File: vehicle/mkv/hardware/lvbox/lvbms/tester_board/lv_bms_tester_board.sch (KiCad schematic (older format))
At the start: 13 parts, among them Q1 SQM110P06, Q2 MMBF170, Q3 SQM110P06, U3 redcube-7461057, U4 redcube-7461057

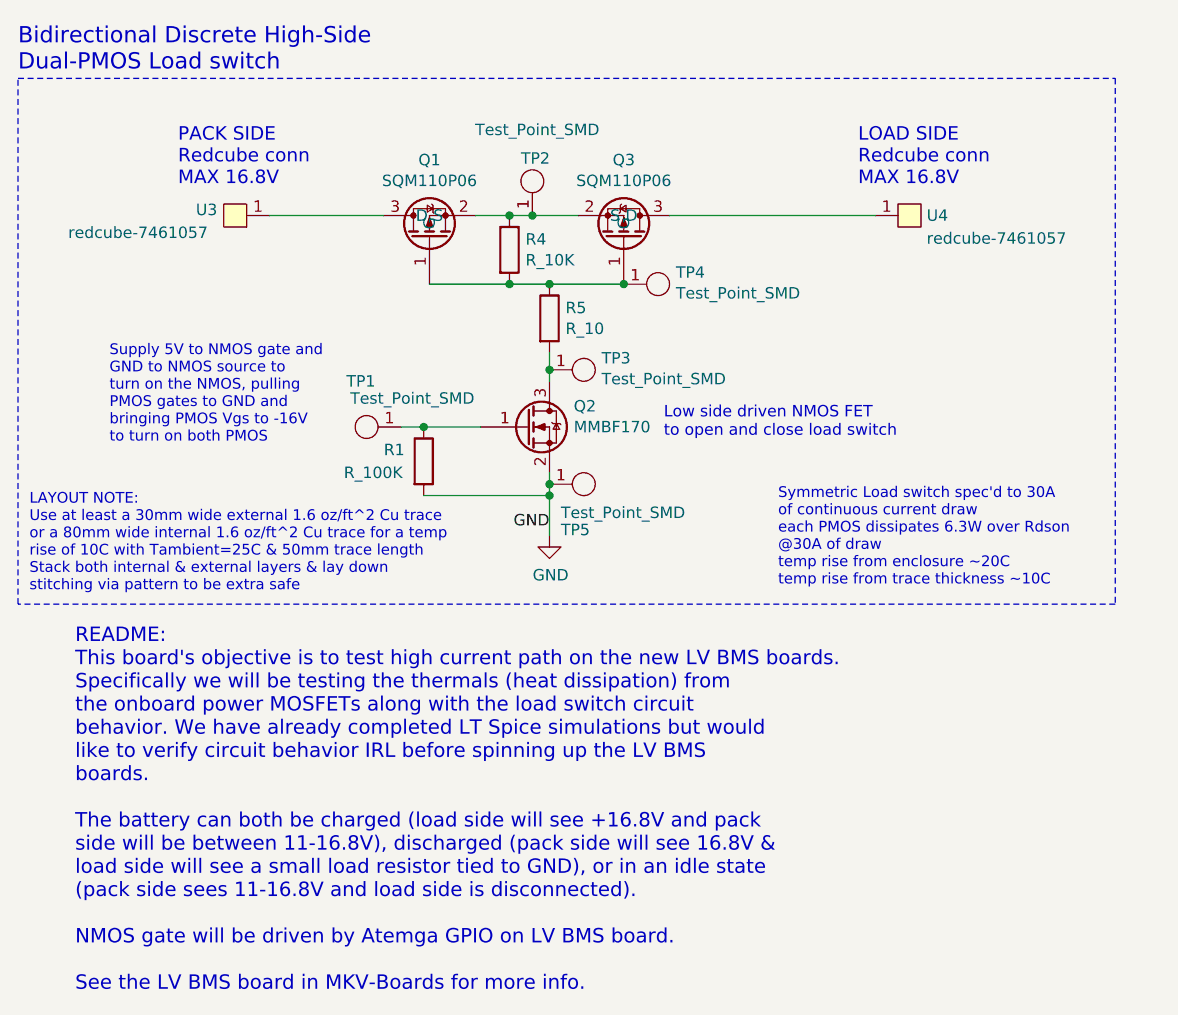
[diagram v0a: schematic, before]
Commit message: Updates based on feedback to LV BMS tester board
Also fixes smudge/clean
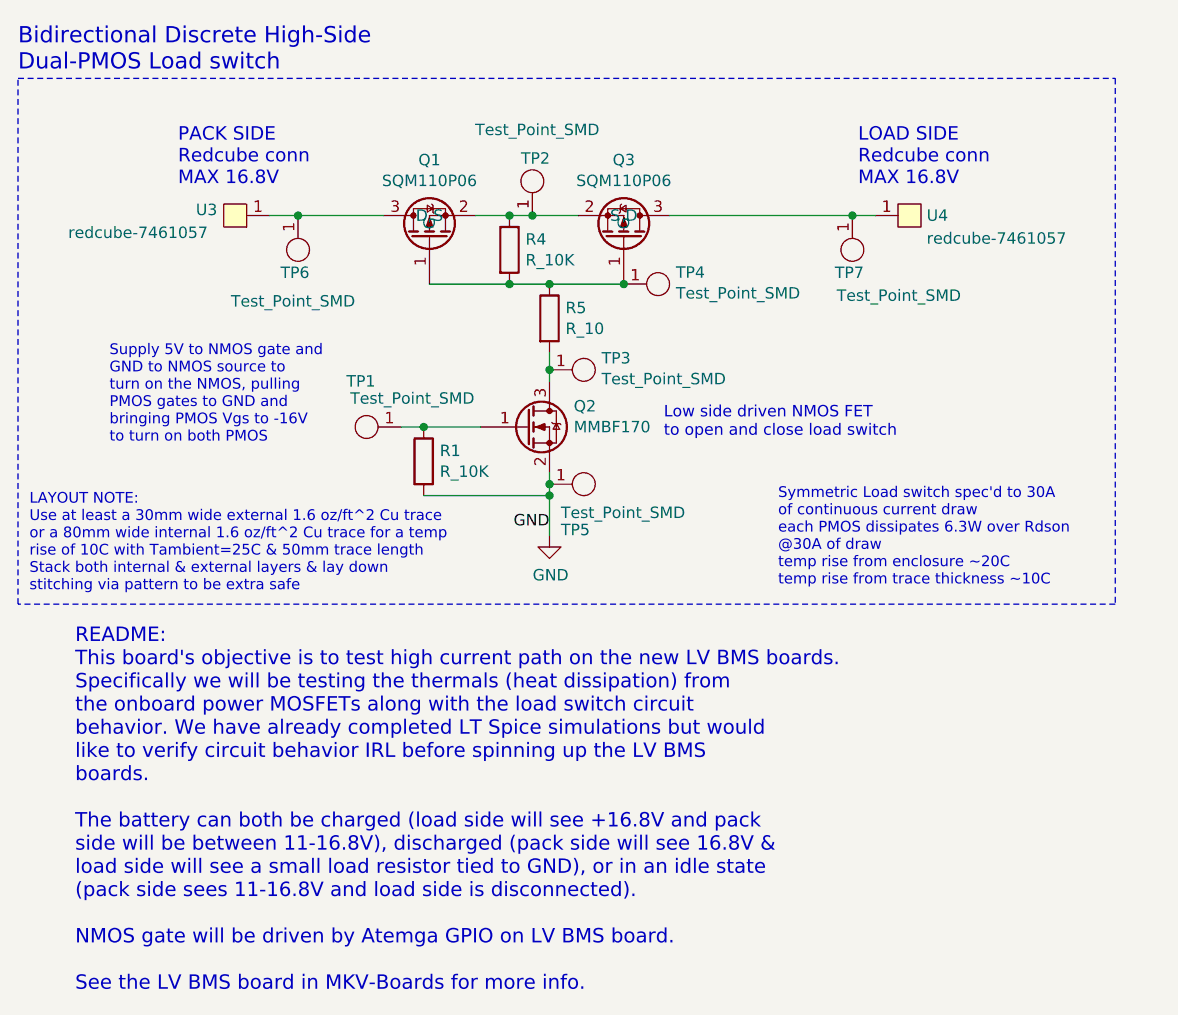
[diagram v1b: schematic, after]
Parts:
- removed R1: R_100K, formula:R_0805_OEM, symbol formula:R_100K
- added R1: R_10K, formula:R_0805_OEM, symbol formula:R_10K
- added TP6, TP7: Test_Point_SMD, TestPoint:TestPoint_Pad_D1.5mm, symbol formula:Test_Point_SMD
- TP1, TP5: footprint TestPoint:TestPoint_Pad_D1.5mm -> TestPoint:TestPoint_Pad_2.0x2.0mm
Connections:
- net GND: now also R1.2
- net at Q1.3 (D), U3.1: now also TP6.1
- net at Q3.3 (D), U4.1: now also TP7.1
- net at Q2.1 (G), TP1.1: now also R1.1
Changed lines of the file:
@@
 $EndComp
 Wire Wire Line
-	3425 1400 4325 1400
-Wire Wire Line
-	1675 1400 2175 1400
+	3425 1400 4225 1400
+Wire Wire Line
+	1675 1400 1800 1400
 $Comp
 L formula:R_10K R4
@@
 	1    0    0    -1
 $EndComp
-Wire Wire Line
-	2600 2325 2350 2325
 $Comp
 L formula:Test_Point_SMD TP1
@@
 F 0 "TP1" V 2400 2450 50  0000 C CNN
 F 1 "Test_Point_SMD" V 2325 2225 50  0000 C CNN
-F 2 "TestPoint:TestPoint_Pad_D1.5mm" H 2200 2175 50  0001 C CNN
+F 2 "TestPoint:TestPoint_Pad_2.0x2.0mm" H 2200 2175 50  0001 C CNN
 F 3 "" H 2200 2325 50  0001 C CNN
 	1    2200 2325
@@
 F 0 "TP5" V 3150 2575 50  0000 L CNN
 F 1 "Test_Point_SMD" V 3075 2575 50  0000 L CNN
-F 2 "TestPoint:TestPoint_Pad_D1.5mm" H 2950 2425 50  0001 C CNN
+F 2 "TestPoint:TestPoint_Pad_2.0x2.0mm" H 2950 2425 50  0001 C CNN
 F 3 "" H 2950 2575 50  0001 C CNN
 	1    2950 2575
@@
 Text Notes 3400 2375 0    50   ~ 0
 Low side driven NMOS FET \nto open and close load switch
-$Comp
-L formula:R_100K R1
-U 1 1 6147C900
-P 2350 2475
-F 0 "R1" H 2175 2525 50  0000 L CNN
-F 1 "R_100K" H 2000 2425 50  0000 L CNN
-F 2 "formula:R_0805_OEM" H 2280 2475 50  0001 C CNN
-F 3 "https://industrial.panasonic.com/cdbs/www-data/pdf/RDA0000/AOA0000C304.pdf" H 2430 2475 50  0001 C CNN
-F 4 "DK" H 2350 2475 60  0001 C CNN "MFN"
-F 5 "P100KCCT-ND" H 2350 2475 60  0001 C CNN "MPN"
-F 6 "https://www.digikey.com/product-detail/en/panasonic-electronic-components/ERJ-6ENF1003V/P100KCCT-ND/119551" H 2830 2875 60  0001 C CNN "PurchasingLink"
-	1    2350 2475
-	1    0    0    -1
-$EndComp
-Connection ~ 2350 2325
-Wire Wire Line
-	2350 2325 2250 2325
 Wire Wire Line
 	2350 2625 2900 2625
@@
 Text Notes 825  4800 0    63   ~ 0
 README: \nThis board's objective is to test high current path on the new LV BMS boards. \nSpecifically we will be testing the thermals (heat dissipation) from\nthe onboard power MOSFETs along with the load switch circuit\nbehavior. We have already completed LT Spice simulations but would\nlike to verify circuit behavior IRL before spinning up the LV BMS\nboards. \n\nThe battery can both be charged (load side will see +16.8V and pack\nside will be between 11-16.8V), discharged (pack side will see 16.8V &\nload side will see a small load resistor tied to GND), or in an idle state\n(pack side sees 11-16.8V and load side is disconnected). \n\nNMOS gate will be driven by Atemga GPIO on LV BMS board. \n\nSee the LV BMS board in MKV-Boards for more info.
+Wire Wire Line
+	2250 2325 2350 2325
+$Comp
+L formula:R_10K R1
+U 1 1 614A6065
+P 2350 2475
+F 0 "R1" H 2420 2521 50  0000 L CNN
+F 1 "R_10K" H 2420 2430 50  0000 L CNN
+F 2 "formula:R_0805_OEM" H 2280 2475 50  0001 C CNN
+F 3 "http://www.bourns.com/data/global/pdfs/CRS.pdf" H 2430 2475 50  0001 C CNN
+F 4 "DK" H 2350 2475 60  0001 C CNN "MFN"
+F 5 "CRS0805-FX-1002ELFCT-ND" H 2350 2475 60  0001 C CNN "MPN"
+F 6 "https://www.digikey.com/products/en?keywords=CRS0805-FX-1002ELFCT-ND" H 2830 2875 60  0001 C CNN "PurchasingLink"
+	1    2350 2475
+	1    0    0    -1
+$EndComp
+Connection ~ 2350 2325
+Wire Wire Line
+	2350 2325 2600 2325
+$Comp
+L formula:Test_Point_SMD TP6
+U 1 1 614A84EE
+P 1800 1450
+F 0 "TP6" H 1750 1650 50  0000 L CNN
+F 1 "Test_Point_SMD" H 1550 1775 50  0000 L CNN
+F 2 "TestPoint:TestPoint_Pad_D1.5mm" H 1800 1300 50  0001 C CNN
+F 3 "" H 1800 1450 50  0001 C CNN
+	1    1800 1450
+	-1   0    0    1
+$EndComp
+$Comp
+L formula:Test_Point_SMD TP7
+U 1 1 614A9C4C
+P 4225 1450
+F 0 "TP7" H 4175 1650 50  0000 L CNN
+F 1 "Test_Point_SMD" H 3750 1750 50  0000 L CNN
+F 2 "TestPoint:TestPoint_Pad_D1.5mm" H 4225 1300 50  0001 C CNN
+F 3 "" H 4225 1450 50  0001 C CNN
+	1    4225 1450
+	-1   0    0    1
+$EndComp
+Connection ~ 4225 1400
+Wire Wire Line
+	4225 1400 4325 1400
+Connection ~ 1800 1400
+Wire Wire Line
+	1800 1400 2175 1400
 $EndSCHEMATC

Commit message: updates for LV BMS Schematic DR
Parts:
- TP1, TP5: footprint TestPoint:TestPoint_Pad_2.0x2.0mm -> formula:Test_Point_SMD
- TP6, TP7: footprint TestPoint:TestPoint_Pad_D1.5mm -> formula:Test_Point_SMD
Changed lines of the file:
@@
 F 0 "TP1" V 2400 2450 50  0000 C CNN
 F 1 "Test_Point_SMD" V 2325 2225 50  0000 C CNN
-F 2 "TestPoint:TestPoint_Pad_2.0x2.0mm" H 2200 2175 50  0001 C CNN
+F 2 "formula:Test_Point_SMD" H 2200 2175 50  0001 C CNN
 F 3 "" H 2200 2325 50  0001 C CNN
 	1    2200 2325
@@
 F 0 "TP5" V 3150 2575 50  0000 L CNN
 F 1 "Test_Point_SMD" V 3075 2575 50  0000 L CNN
-F 2 "TestPoint:TestPoint_Pad_2.0x2.0mm" H 2950 2425 50  0001 C CNN
+F 2 "formula:Test_Point_SMD" H 2950 2425 50  0001 C CNN
 F 3 "" H 2950 2575 50  0001 C CNN
 	1    2950 2575
@@
 F 0 "TP6" H 1750 1650 50  0000 L CNN
 F 1 "Test_Point_SMD" H 1550 1775 50  0000 L CNN
-F 2 "TestPoint:TestPoint_Pad_D1.5mm" H 1800 1300 50  0001 C CNN
+F 2 "formula:Test_Point_SMD" H 1800 1300 50  0001 C CNN
 F 3 "" H 1800 1450 50  0001 C CNN
 	1    1800 1450
@@
 F 0 "TP7" H 4175 1650 50  0000 L CNN
 F 1 "Test_Point_SMD" H 3750 1750 50  0000 L CNN
-F 2 "TestPoint:TestPoint_Pad_D1.5mm" H 4225 1300 50  0001 C CNN
+F 2 "formula:Test_Point_SMD" H 4225 1300 50  0001 C CNN
 F 3 "" H 4225 1450 50  0001 C CNN
 	1    4225 1450
